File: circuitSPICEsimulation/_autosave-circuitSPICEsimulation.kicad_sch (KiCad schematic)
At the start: 31 parts, among them U1 ${SIM.PARAMS}, U2 ${SIM.PARAMS}, U3 ${SIM.PARAMS}, U4 ${SIM.PARAMS}, U6 ${SIM.PARAMS}

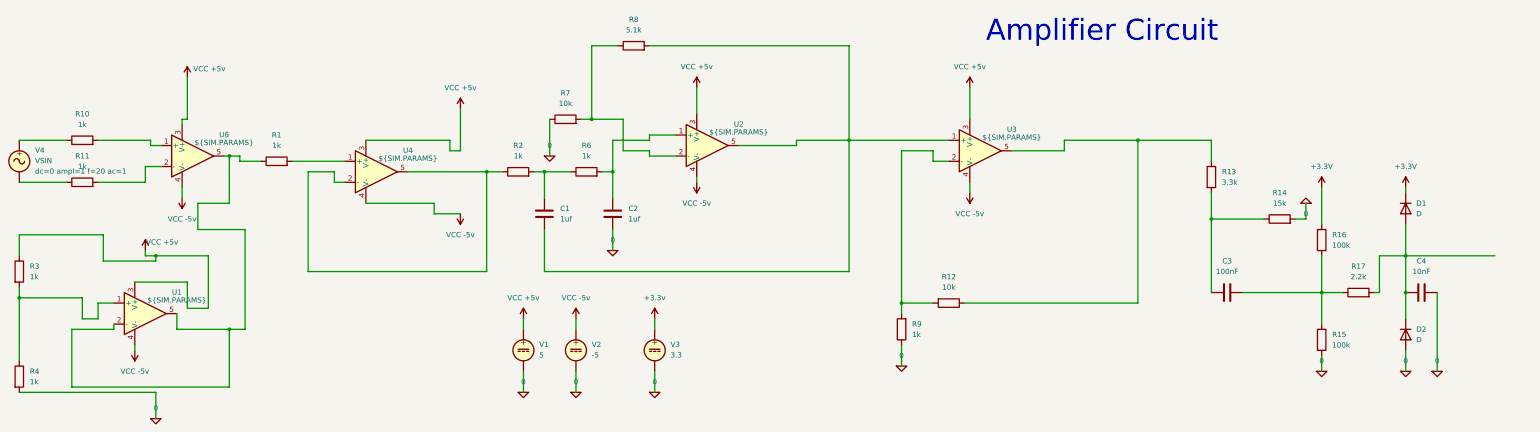
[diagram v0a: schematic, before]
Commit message: changed the frequency, added the attenuation circuit and expirementing on that
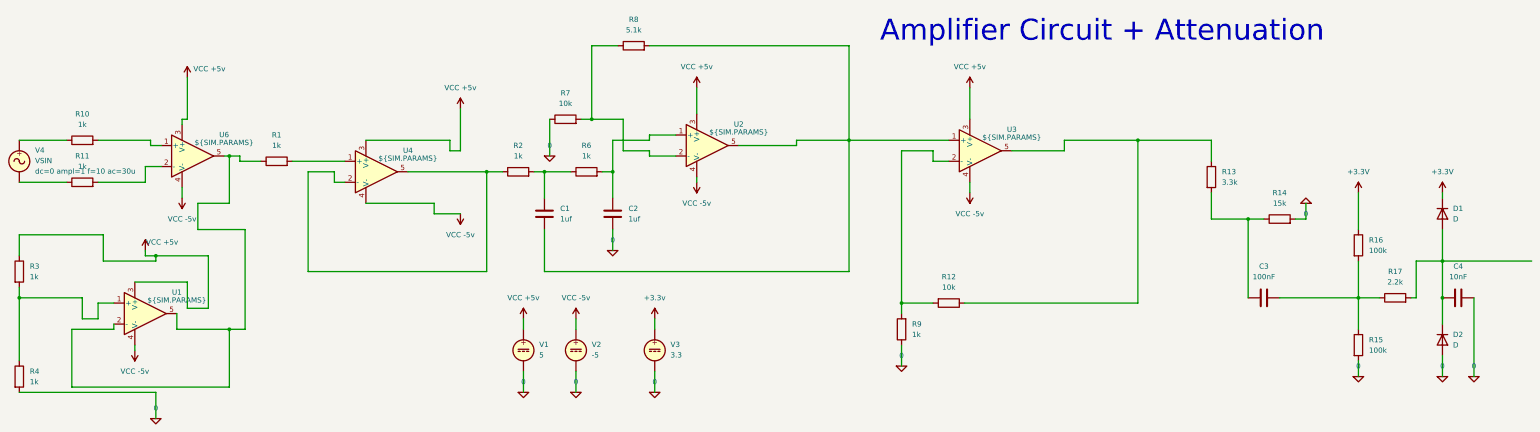
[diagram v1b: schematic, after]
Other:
- note added: "Amplifier Circuit + Attenuation"
- note removed: "Amplifier Circuit"
- moved on the sheet: C3, C4, D1, D2, R15, R16, R17
